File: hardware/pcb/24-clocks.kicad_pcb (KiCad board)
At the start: 2 copper layers, 94 x 94 mm, 97 parts, among them J201 ST-LINK, J202 Debug UART, J401 S4B_XH_SM4_TB, J402 S4B_XH_SM4_TB, J601 Conn_02x03_Odd_Even, U201 STM32F103C8Tx, U301 VID28-05, U302 VID66-08, U303 AH3572, U304 AH3572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

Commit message: First placement
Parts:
- removed TP211: HW-Version, TestPoint:TestPoint_Pad_D2.0mm
- removed TP301: MA1, TestPoint:TestPoint_Pad_D2.0mm
- removed TP302: MA2, TestPoint:TestPoint_Pad_D2.0mm
- removed TP304: MA3, TestPoint:TestPoint_Pad_D2.0mm
- removed TP307: MA4, TestPoint:TestPoint_Pad_D2.0mm
- removed TP310: MB1, TestPoint:TestPoint_Pad_D2.0mm
- removed TP311: MB2, TestPoint:TestPoint_Pad_D2.0mm
- removed TP312: MB3, TestPoint:TestPoint_Pad_D2.0mm
- removed TP313: MB4, TestPoint:TestPoint_Pad_D2.0mm
- moved TP306 204.2 mm to (165.2, 117.8)
- moved TP315 200.7 mm to (147.5, 125.4)
- moved TP601 200.6 mm to (142.4, 117.8)
- moved TP602 195.0 mm to (142.4, 122.9)
- moved TP314 191.6 mm to (147.5, 115.2)
- moved TP210 190.9 mm to (119.5, 122.9)
- moved TP309 189.2 mm to (165.2, 107.6)
- moved TP303 188.5 mm to (165.2, 97.5)
- moved TP209 186.2 mm to (117.0, 117.8)
- moved TP308 183.3 mm to (165.2, 102.5)
- moved TP305 179.2 mm to (165.2, 112.7)
- moved TP701 171.9 mm to (122.1, 130.5)
- moved TP203 171.4 mm to (122.1, 89.8)
- moved TP204 164.2 mm to (122.1, 94.9)
- moved TP201 162.7 mm to (122.1, 84.8)
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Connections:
- net +9V renamed +7.5V
- J202 pad 2: (no net) -> Net-(J202-Pad2)
- J202 pad 6: (no net) -> Net-(J202-Pad6)
- U201 pad 10: (no net) -> Net-(U201-Pad10)
- U201 pad 14: (no net) -> Net-(U201-Pad14)
- U201 pad 15: (no net) -> Net-(U201-Pad15)
- U201 pad 18: (no net) -> Net-(U201-Pad18)
- U201 pad 19: (no net) -> Net-(U201-Pad19)
- U201 pad 2: (no net) -> Net-(U201-Pad2)
- U201 pad 25: (no net) -> Net-(U201-Pad25)
- U201 pad 29: (no net) -> Net-(U201-Pad29)
- U201 pad 3: (no net) -> Net-(U201-Pad3)
- U201 pad 32: (no net) -> Net-(U201-Pad32)
- U201 pad 4: (no net) -> Net-(U201-Pad4)
- U201 pad 40: (no net) -> Net-(U201-Pad40)
- U201 pad 41: (no net) -> Net-(U201-Pad41)
- U201 pad 46: (no net) -> Net-(U201-Pad46)
- U601 pad 10: (no net) -> Net-(U601-Pad10)
- U601 pad 11: (no net) -> Net-(U601-Pad11)
- U601 pad 12: (no net) -> Net-(U601-Pad12)
- U601 pad 13: (no net) -> Net-(U601-Pad13)
- U601 pad 14: (no net) -> Net-(U601-Pad14)
- U601 pad 16: (no net) -> Net-(U601-Pad16)
- U601 pad 17: (no net) -> Net-(U601-Pad17)
- U601 pad 18: (no net) -> Net-(U601-Pad18)
- U601 pad 19: (no net) -> Net-(U601-Pad19)
- U601 pad 20: (no net) -> Net-(U601-Pad20)
- U601 pad 21: (no net) -> Net-(U601-Pad21)
- U601 pad 22: (no net) -> Net-(U601-Pad22)
- U601 pad 23: (no net) -> Net-(U601-Pad23)
- U601 pad 24: (no net) -> Net-(U601-Pad24)
- U601 pad 26: (no net) -> Net-(U601-Pad26)
- U601 pad 29: (no net) -> Net-(U601-Pad29)
- U601 pad 30: (no net) -> Net-(U601-Pad30)
- U601 pad 31: (no net) -> Net-(U601-Pad31)
- U601 pad 32: (no net) -> Net-(U601-Pad32)
- U601 pad 33: (no net) -> Net-(U601-Pad33)
- U601 pad 36: (no net) -> Net-(U601-Pad36)
- U601 pad 37: (no net) -> Net-(U601-Pad37)
- U601 pad 4: (no net) -> Net-(U601-Pad4)
- U601 pad 5: (no net) -> Net-(U601-Pad5)
- U601 pad 6: (no net) -> Net-(U601-Pad6)
- U601 pad 7: (no net) -> Net-(U601-Pad7)
- U601 pad 8: (no net) -> Net-(U601-Pad8)
- U601 pad 9: (no net) -> Net-(U601-Pad9)
- U701 pad 7: (no net) -> Net-(U701-Pad7)
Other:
- rule pad_to_mask_clearance: 0.051 -> 0

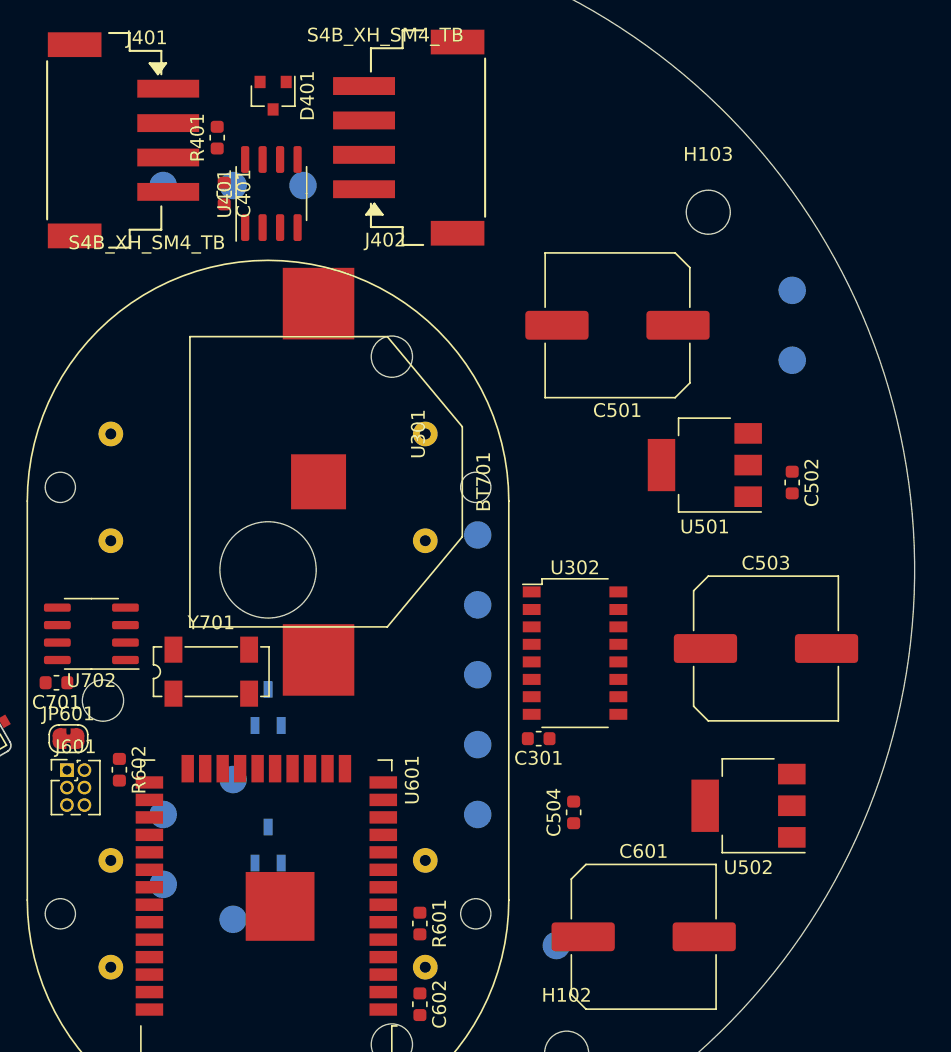
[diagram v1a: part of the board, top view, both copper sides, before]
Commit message: Routed supplies
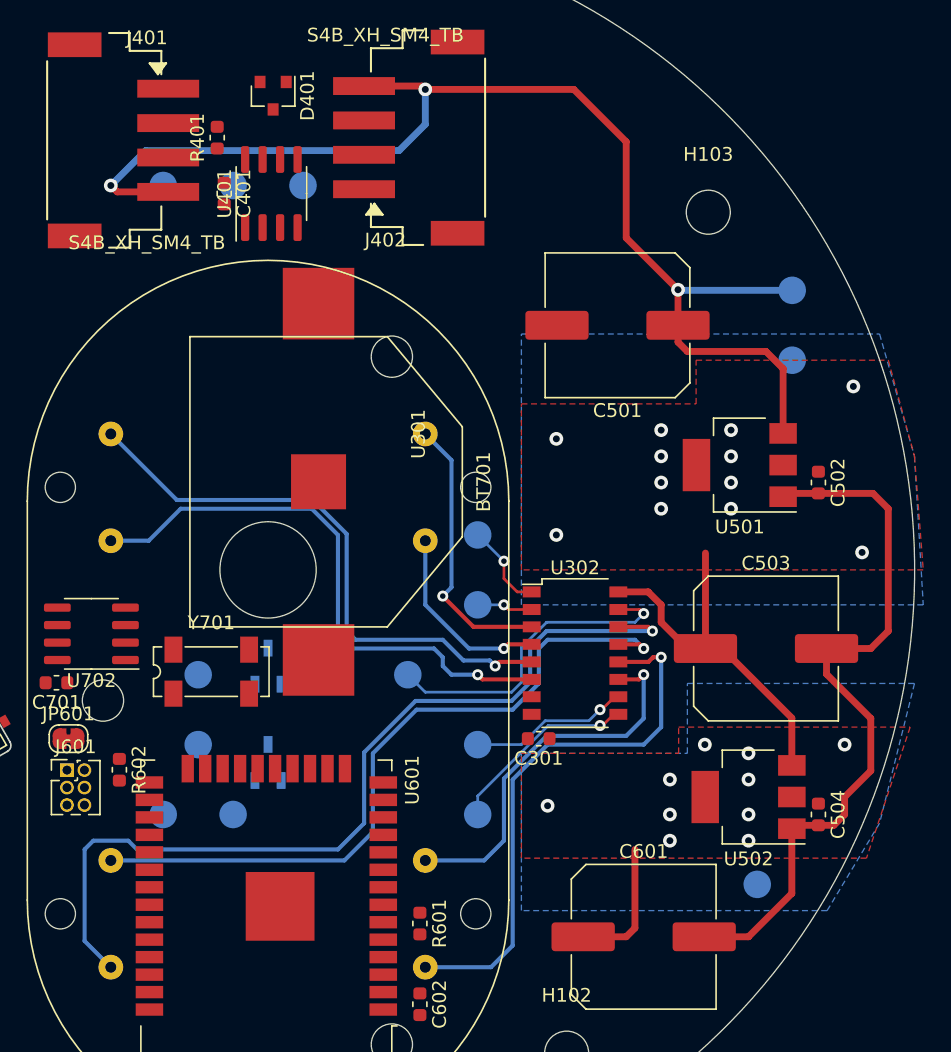
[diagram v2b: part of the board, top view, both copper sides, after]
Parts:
- moved C504 17.8 mm to (190.0, 117.8), turned to 270 degrees
- moved TP503 15.3 mm to (185.6, 122.9)
- moved TP315 13.0 mm to (144.9, 112.7)
- moved TP303 11.4 mm to (160.2, 107.6)
- moved TP314 8.03 mm to (144.9, 107.6)
- moved TP602 7.18 mm to (147.5, 117.8)
- moved U306 6.00 mm to (150.0, 114.0)
- moved TP308 5.08 mm to (165.2, 97.5)
- moved TP305 5.08 mm to (165.2, 117.8)
- moved TP306 5.08 mm to (165.2, 112.7)
- moved TP309 5.08 mm to (165.2, 102.5)
- moved U305 3.00 mm to (150.0, 107.0)
- moved U501 2.54 mm to (184.3, 92.4)
- moved C502 1.91 mm to (190.0, 93.7)
- moved U502 0.63 mm to (184.9, 116.5)
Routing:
- net +7.5V: track 0.00 -> 89.9 mm, vias 0 -> 3
- net /Mechanics/MB3: track 0.00 -> 64.8 mm, vias 0 -> 1
- net GND: track 0.00 -> 52.9 mm
- net /Mechanics/MB4: track 0.00 -> 52.4 mm, vias 0 -> 1
- net /Mechanics/MA4: track 0.00 -> 41.8 mm, vias 0 -> 1
- net /Mechanics/MA3: track 0.00 -> 41.5 mm, vias 0 -> 1
- net /Mechanics/MB2: track 0.00 -> 39.8 mm, vias 0 -> 1
- net /Mechanics/MB1: track 0.00 -> 28.0 mm, vias 0 -> 1
- net +5V: track 0.00 -> 27.5 mm, vias 0 -> 12
- net /Mechanics/M-Rst: track 0.00 -> 23.5 mm, vias 0 -> 1
- net /Mechanics/MA1: track 0.00 -> 20.2 mm, vias 0 -> 1
- net /Mechanics/M-A-CW: track 0.00 -> 14.0 mm, vias 0 -> 1
- net /Mechanics/MA2: track 0.00 -> 13.8 mm, vias 0 -> 1
- net /Mechanics/M-A-Step: track 0.00 -> 11.7 mm, vias 0 -> 1
- net +3V3: track 0.00 -> 9.74 mm, vias 0 -> 10
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- added copper zone on B.Cu, net +3V3
- added copper zone on F.Cu, net +3V3
- added copper zone on B.Cu, net +5V
- added copper zone on F.Cu, net +5V
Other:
- net class Default: clearance 0.2 -> 0.15; trace_width 0.25 -> 0.2
- net class Motor added: clearance 0.2, trace_width 0.3, via_dia 0.8, via_drill 0.4
- net class Power added: clearance 0.2, trace_width 0.5, via_dia 1, via_drill 0.5
- net class RS485 added: clearance 0.2, trace_width 0.3, via_dia 0.8, via_drill 0.4
- rule trace_clearance: 0.2 -> 0.15

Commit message: Update 24-clocks.kicad_pcb
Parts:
- moved JP203 12.1 mm to (111.9, 97.5)
- moved TP504 5.08 mm to (150.0, 61.9)
- moved JP202 1.41 mm to (114.4, 116.5), turned to 207 degrees
- moved JP201 0.89 mm to (117.6, 81.6), turned to 157 degrees
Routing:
- net +3V3: track 9.74 -> 131.2 mm, vias 10 -> 11
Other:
- board size 94 x 94 mm -> 94 x 84 mm

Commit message: Added routing
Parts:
- moved R203 18.5 mm to (106.8, 95.6), turned to 90 degrees
- moved TP202 18.0 mm to (109.4, 92.4)
- moved TP208 14.8 mm to (114.4, 92.4)
- moved R202 10.4 mm to (117.0, 93.7), turned to 90 degrees
- moved U702 8.12 mm to (129.0, 104.4)
- moved Y701 8.11 mm to (137.9, 105.7)
- moved C701 6.84 mm to (127.8, 108.2), turned to 0 degrees
- moved R201 5.69 mm to (109.4, 96.2), turned to 270 degrees
- moved R701 5.51 mm to (124.0, 105.7), turned to 90 degrees
- moved C401 0.69 mm to (146.8, 73.3)
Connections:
- net Net-(BT701-Pad1) renamed /RTC and Memory/Vbat
- R701 pad 2: /RTC and Memory/RCLK -> /RTC and Memory/RTC-CLK
- U201 pad 25: Net-(U201-Pad25) -> /RTC and Memory/RTC-CLK
- U702 pad 7: /RTC and Memory/RCLK -> /RTC and Memory/RTC-CLK
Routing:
- net +3V3: track 131.2 -> 267.5 mm, vias 11 -> 20
- net /RTC and Memory/Vbat: track 0.00 -> 62.6 mm, vias 0 -> 1
- net /Com Bus/uC-RS485-DE: track 0.00 -> 61.7 mm, vias 0 -> 2
- net /Com Bus/uC-RS485-Tx: track 0.00 -> 60.2 mm, vias 0 -> 2
- net /Com Bus/uC-RS485-Rx: track 0.00 -> 55.3 mm, vias 0 -> 2
- net /Mechanics/HAL-B: track 0.00 -> 54.5 mm, vias 0 -> 1
- net /Mechanics/HAL-A: track 0.00 -> 45.1 mm, vias 0 -> 3
- net /WiFi/uC-WiFi-Rx: track 0.00 -> 36.5 mm, vias 0 -> 1
- net /WiFi/uC-WiFi-Tx: track 0.00 -> 35.4 mm, vias 0 -> 2
- net /uC/SWDIO: track 0.00 -> 34.8 mm, vias 0 -> 1
- net /uC/SWO: track 0.00 -> 28.9 mm, vias 0 -> 1
- net /uC/uC-RST: track 0.00 -> 28.7 mm, vias 0 -> 3
- net /uC/BOOT1: track 0.00 -> 28.7 mm, vias 0 -> 2
- net /uC/SWDCLK: track 0.00 -> 27.2 mm, vias 0 -> 1
- net /Com Bus/RS485-A: track 0.00 -> 21.4 mm, vias 0 -> 2
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- added copper zone on B.Cu, net GND
- added copper zone on F.Cu, net GND

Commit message: Routed more nets
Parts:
- moved R102 3.49 mm to (130.2, 122.4), turned to 180 degrees
- moved R101 3.42 mm to (130.2, 123.9), turned to 180 degrees
- moved J202 0.13 mm to (109.4, 113.2)
- turned C301 to 0 degrees
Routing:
- net /Mechanics/M-A-CW: track 14.0 -> 79.1 mm, vias 1 -> 4
- net /I2C-SDA: track 18.4 -> 78.8 mm, vias 0 -> 4
- net /Mechanics/M-Rst: track 23.5 -> 82.5 mm, vias 1 -> 2
- net /I2C-SCL: track 19.0 -> 75.6 mm, vias 0 -> 4
- net /Mechanics/M-A-Step: track 30.6 -> 86.9 mm, vias 1 -> 4
- net /Mechanics/M-B-CW: track 6.38 -> 60.7 mm, vias 1 -> 3
- net /Mechanics/M-B-Step: track 18.2 -> 64.9 mm, vias 2 -> 5
- net /WiFi/ESP-EN: track 0.00 -> 41.0 mm
- net /uC/uC-Debug-Tx: track 0.00 -> 31.6 mm
- net +3V3: track 267.5 -> 295.5 mm, vias 20 -> 23
- net /uC/uC-Debug-Rx: track 0.00 -> 21.0 mm, vias 0 -> 1
- net +5V: track 27.5 -> 47.5 mm
- net /WiFi/ESP-IO0: track 0.00 -> 6.15 mm
- net /Mechanics/MA3: track 41.5 -> 44.9 mm
- net /Com Bus/uC-RS485-Tx: track 60.2 -> 58.2 mm
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
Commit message: Finished routing
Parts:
- added NT701: Net-Tie_2, NetTie:NetTie-2_SMD_Pad0.5mm, F.Cu at (129.7, 101.5)
- U301: footprint mvl-footprints:vid_28_05 -> mvl-footprints:BK30D-R5
- moved C702 21.2 mm to (128.2, 108.1), turned to 0 degrees
- moved C701 19.5 mm to (123.3, 127.2), turned to 270 degrees
- moved TP401 2.54 mm to (147.5, 74.6)
- moved TP402 2.54 mm to (142.4, 74.6)
- moved TP403 2.54 mm to (152.5, 74.6)
- moved R101 1.52 mm to (130.2, 122.4)
- moved R102 1.52 mm to (130.2, 120.8)
- moved U701 1.52 mm to (127.0, 127.4)
- moved JP601 0.79 mm to (136.3, 112.3)
- moved C401 0.37 mm to (146.4, 73.3)
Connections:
- C702 pad 2: GND -> /RTC and Memory/GND-CLK
- J202 pad 2: Net-(J202-Pad2) -> (no net)
- J202 pad 6: Net-(J202-Pad6) -> (no net)
- U201 pad 10: Net-(U201-Pad10) -> (no net)
- U201 pad 14: Net-(U201-Pad14) -> (no net)
- U201 pad 15: Net-(U201-Pad15) -> (no net)
- U201 pad 18: Net-(U201-Pad18) -> (no net)
- U201 pad 19: Net-(U201-Pad19) -> (no net)
- U201 pad 2: Net-(U201-Pad2) -> (no net)
- U201 pad 29: Net-(U201-Pad29) -> (no net)
- U201 pad 3: Net-(U201-Pad3) -> (no net)
- U201 pad 32: Net-(U201-Pad32) -> (no net)
- U201 pad 4: Net-(U201-Pad4) -> (no net)
- U201 pad 40: Net-(U201-Pad40) -> (no net)
- U201 pad 41: Net-(U201-Pad41) -> (no net)
- U201 pad 46: Net-(U201-Pad46) -> (no net)
- U601 pad 10: Net-(U601-Pad10) -> (no net)
- U601 pad 11: Net-(U601-Pad11) -> (no net)
- U601 pad 12: Net-(U601-Pad12) -> (no net)
- U601 pad 13: Net-(U601-Pad13) -> (no net)
- U601 pad 14: Net-(U601-Pad14) -> (no net)
- U601 pad 16: Net-(U601-Pad16) -> (no net)
- U601 pad 17: Net-(U601-Pad17) -> (no net)
- U601 pad 18: Net-(U601-Pad18) -> (no net)
- U601 pad 19: Net-(U601-Pad19) -> (no net)
- U601 pad 20: Net-(U601-Pad20) -> (no net)
- U601 pad 21: Net-(U601-Pad21) -> (no net)
- U601 pad 22: Net-(U601-Pad22) -> (no net)
- U601 pad 23: Net-(U601-Pad23) -> (no net)
- U601 pad 24: Net-(U601-Pad24) -> (no net)
- U601 pad 26: Net-(U601-Pad26) -> (no net)
- U601 pad 29: Net-(U601-Pad29) -> (no net)
- U601 pad 30: Net-(U601-Pad30) -> (no net)
- U601 pad 31: Net-(U601-Pad31) -> (no net)
- U601 pad 32: Net-(U601-Pad32) -> (no net)
- U601 pad 33: Net-(U601-Pad33) -> (no net)
- U601 pad 36: Net-(U601-Pad36) -> (no net)
- U601 pad 37: Net-(U601-Pad37) -> (no net)
- U601 pad 4: Net-(U601-Pad4) -> (no net)
- U601 pad 5: Net-(U601-Pad5) -> (no net)
- U601 pad 6: Net-(U601-Pad6) -> (no net)
- U601 pad 7: Net-(U601-Pad7) -> (no net)
- U601 pad 8: Net-(U601-Pad8) -> (no net)
- U601 pad 9: Net-(U601-Pad9) -> (no net)
- U701 pad 7: Net-(U701-Pad7) -> (no net)
- U702 pad 4: GND -> /RTC and Memory/GND-CLK
- Y701 pad 2: GND -> /RTC and Memory/GND-CLK
- Y701 pad 3: GND -> /RTC and Memory/GND-CLK
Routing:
- net GND: track 63.8 -> 86.2 mm, vias 6 -> 133
- net /WiFi/ESP-TxD0: track 0.00 -> 20.2 mm, vias 0 -> 1
- net +3V3: track 295.5 -> 313.7 mm
- net /WiFi/ESP-RxD0: track 0.00 -> 14.9 mm, vias 0 -> 1
- net /uC/BOOT1: track 28.7 -> 34.8 mm
- net Net-(J601-Pad2): track 0.00 -> 3.01 mm
- net /Com Bus/uC-RS485-Tx: track 58.2 -> 55.7 mm
- net /Com Bus/uC-RS485-Rx: track 53.4 -> 50.9 mm
- net /Com Bus/uC-RS485-DE: track 60.0 -> 57.5 mm
- net /RTC and Memory/GND-CLK: track 0.00 -> 2.23 mm, vias 0 -> 3
- net /I2C-SCL: track 75.6 -> 77.4 mm
- net /uC/uC-RST: track 28.7 -> 27.8 mm
- net +7.5V: track 89.9 -> 89.2 mm
- net /Mechanics/HAL-B: track 54.5 -> 55.2 mm
- net /WiFi/ESP-EN: track 41.0 -> 41.1 mm, vias 0 -> 1
- added copper zone on F.Cu, net /RTC and Memory/GND-CLK
- added copper zone on B.Cu, net /RTC and Memory/RTC-CLK
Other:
- board text added: "24 Clocks"
- board text added: "Martin vL"
- board text added: "[GITHASH]"
- board text added: "[dd-mm-yyyy]"
